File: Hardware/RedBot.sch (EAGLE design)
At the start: 66 parts, among them U1 ATMEGA328P, U2 TB6612FNG, U3 MIC5219 5V, U4 MIC5219 3.3V, U5 FT232RLSSOP, U6 7408SE, Y1 16MHz

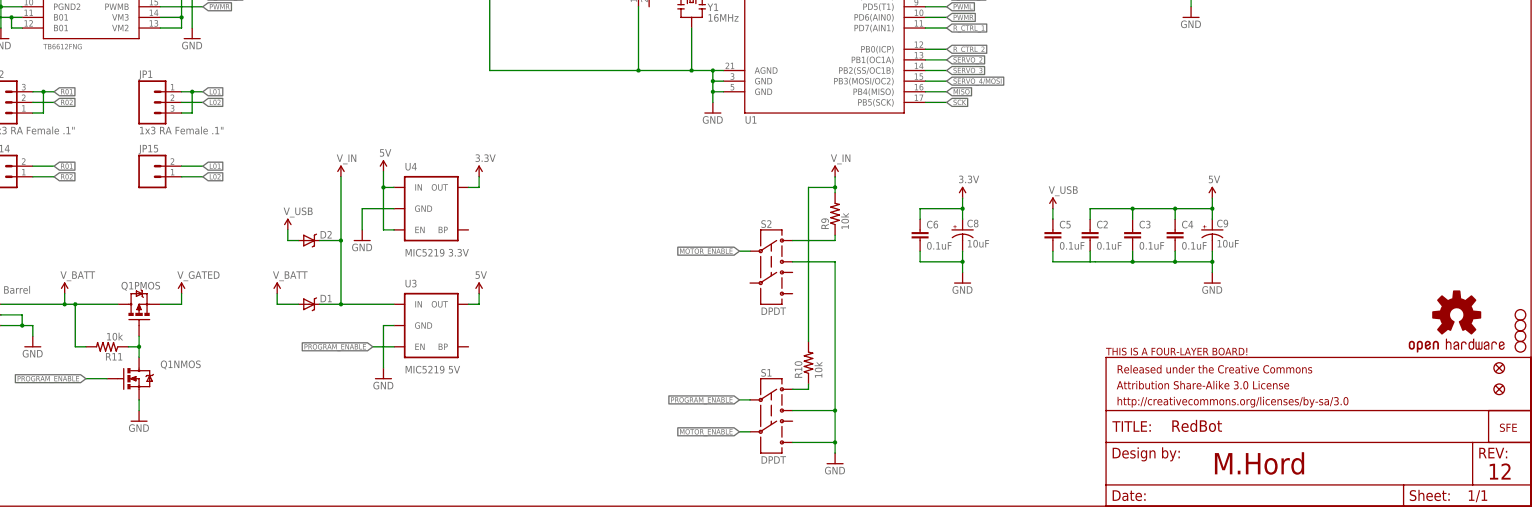
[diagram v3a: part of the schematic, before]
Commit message: Hardware to v13 - Fix gating of battery voltage to servos - Add a user input button to pin 12 - label user led as D13 LED for clarity
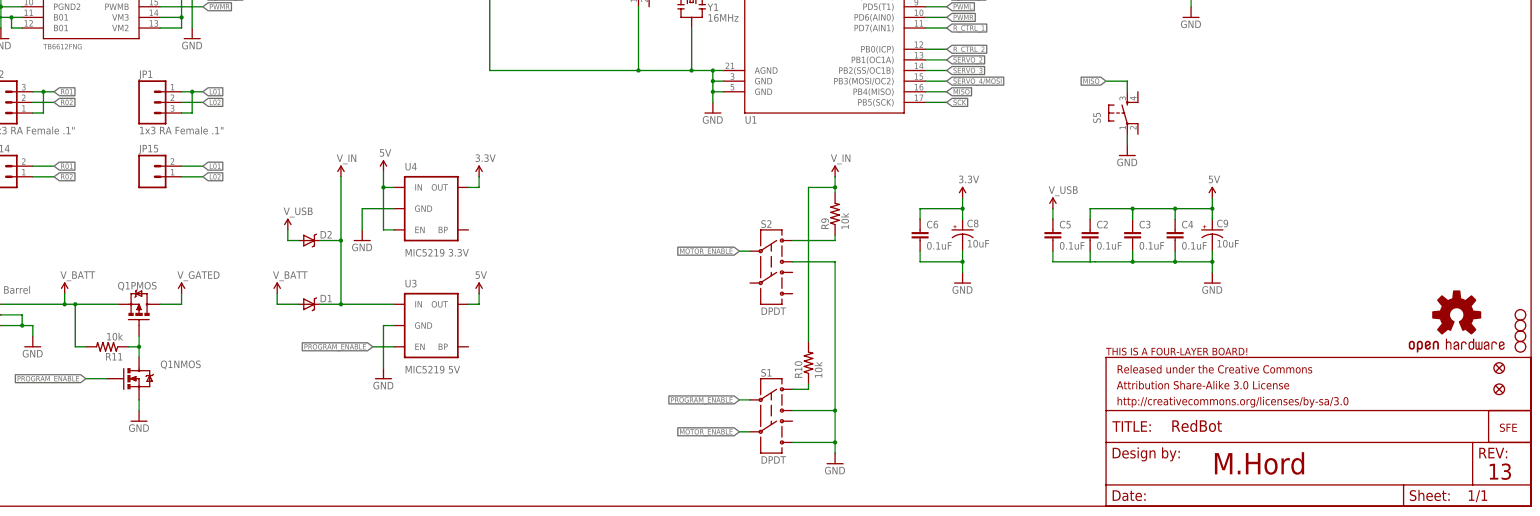
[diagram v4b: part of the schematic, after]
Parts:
- added S5: (no value), SparkFun-Electromechanical:TAC_SWITCHSMD
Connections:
- net GND: now also S5.1
- net MISO: now also S5.3
- net V_BATT: now also Q1PMOS.S; no longer Q1PMOS.D
- net V_GATED: now also Q1PMOS.D; no longer Q1PMOS.S
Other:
- note added: "13"
- note removed: "12"
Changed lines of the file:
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@@
 <part name="FID2" library="SparkFun-Aesthetics" deviceset="FIDUCIAL" device="UFIDUCIAL"/>
 <part name="U$22" library="SparkFun-Aesthetics" deviceset="5V" device="" value="V_USB"/>
+<part name="S5" library="SparkFun-Electromechanical" deviceset="TAC_SWITCH" device="SMD"/>
+<part name="GND12" library="SparkFun-Aesthetics" deviceset="GND" device=""/>
 </parts>
 <sheets>
@@
 <wire x1="0" y1="254" x2="0" y2="0" width="0.1524" layer="94"/>
 <text x="330.2" y="7.62" size="5.08" layer="94">M.Hord</text>
-<text x="395.986" y="6.35" size="3.81" layer="94">12</text>
+<text x="395.986" y="6.35" size="3.81" layer="94">13</text>
 </plain>
 <instances>
@@
 <instance part="JP15" gate="G$1" x="76.2" y="78.74"/>
 <instance part="Q1" gate="NMOS" x="73.66" y="30.48"/>
-<instance part="Q1" gate="PMOS" x="73.66" y="48.26" smashed="yes" rot="R90">
-<attribute name="NAME" x="69.342" y="51.816" size="1.778" layer="95"/>
-<attribute name="VALUE" x="73.66" y="53.34" size="1.778" layer="96" rot="R90"/>
+<instance part="Q1" gate="PMOS" x="73.66" y="48.26" smashed="yes" rot="MR90">
+<attribute name="NAME" x="77.978" y="51.816" size="1.778" layer="95" rot="MR0"/>
+<attribute name="VALUE" x="73.66" y="53.34" size="1.778" layer="96" rot="MR90"/>
 </instance>
 <instance part="GND19" gate="1" x="73.66" y="20.32"/>
@@
 <instance part="FID2" gate="G$1" x="398.78" y="27.94"/>
 <instance part="U$22" gate="G$1" x="144.78" y="195.58"/>
+<instance part="S5" gate="S" x="309.88" y="93.98" rot="R90"/>
+<instance part="GND12" gate="1" x="309.88" y="83.82"/>
 </instances>
 <busses>
@@
 <wire x1="20.32" y1="208.28" x2="15.24" y2="208.28" width="0.1524" layer="91"/>
 <label x="15.24" y="208.28" size="1.27" layer="95" rot="R180" xref="yes"/>
+</segment>
+<segment>
+<pinref part="S5" gate="S" pin="3"/>
+<wire x1="309.88" y1="99.06" x2="309.88" y2="101.6" width="0.1524" layer="91"/>
+<wire x1="309.88" y1="101.6" x2="304.8" y2="101.6" width="0.1524" layer="91"/>
+<label x="304.8" y="101.6" size="1.27" layer="95" rot="R180" xref="yes"/>
 </segment>
 </net>
@@
 <wire x1="27.94" y1="22.86" x2="27.94" y2="20.32" width="0.1524" layer="91"/>
 </segment>
+<segment>
+<pinref part="GND12" gate="1" pin="GND"/>
+<pinref part="S5" gate="S" pin="1"/>
+<wire x1="309.88" y1="86.36" x2="309.88" y2="88.9" width="0.1524" layer="91"/>
+</segment>
 </net>
 <net name="5V" class="0">
@@
 <wire x1="60.96" y1="38.1" x2="58.42" y2="38.1" width="0.1524" layer="91"/>
 <wire x1="58.42" y1="38.1" x2="58.42" y2="48.26" width="0.1524" layer="91"/>
-<pinref part="Q1" gate="PMOS" pin="D"/>
-<wire x1="58.42" y1="48.26" x2="68.58" y2="48.26" width="0.1524" layer="91"/>
-<junction x="58.42" y="48.26"/>
 <wire x1="40.64" y1="48.26" x2="55.88" y2="48.26" width="0.1524" layer="91"/>
 <pinref part="U$18" gate="G$1" pin="V_BATT"/>
@@
 <wire x1="55.88" y1="50.8" x2="55.88" y2="48.26" width="0.1524" layer="91"/>
 <junction x="55.88" y="48.26"/>
+<pinref part="Q1" gate="PMOS" pin="S"/>
+<wire x1="68.58" y1="48.26" x2="58.42" y2="48.26" width="0.1524" layer="91"/>
+<junction x="58.42" y="48.26"/>
 </segment>
 <segment>
@@
 <net name="V_GATED" class="0">
 <segment>
-<pinref part="Q1" gate="PMOS" pin="S"/>
-<wire x1="78.74" y1="48.26" x2="83.82" y2="48.26" width="0.1524" layer="91"/>
 <pinref part="V_GATE1" gate="G$1" pin="V_BATT"/>
 <wire x1="83.82" y1="50.8" x2="83.82" y2="48.26" width="0.1524" layer="91"/>
-</segment>
-<segment>
+<pinref part="Q1" gate="PMOS" pin="D"/>
+<wire x1="78.74" y1="48.26" x2="83.82" y2="48.26" width="0.1524" layer="91"/>
+</segment>
+<segment>

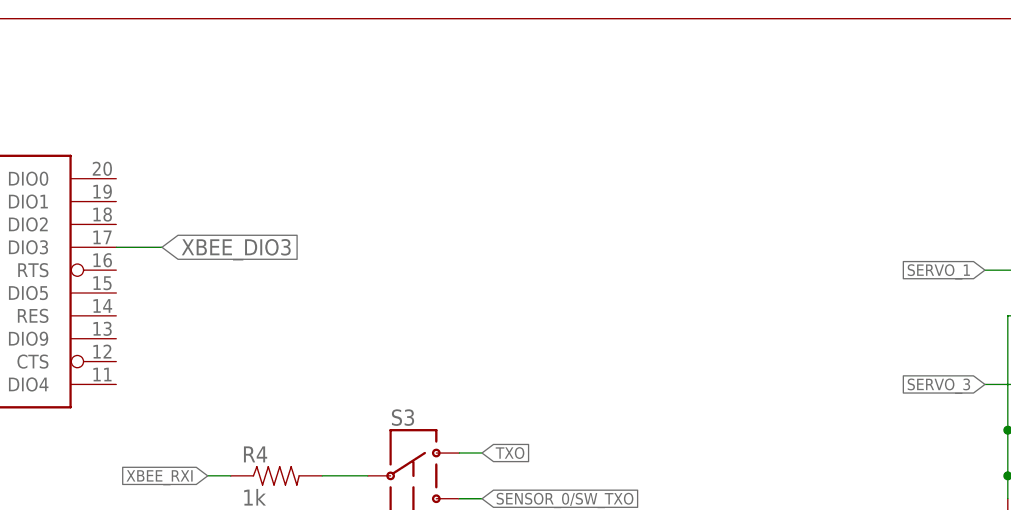
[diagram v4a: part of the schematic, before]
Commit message: Added support for encoder and whisker bumper; changing schematic and layout to fix some issues and pretty it up a bit. Hardware changes not done!
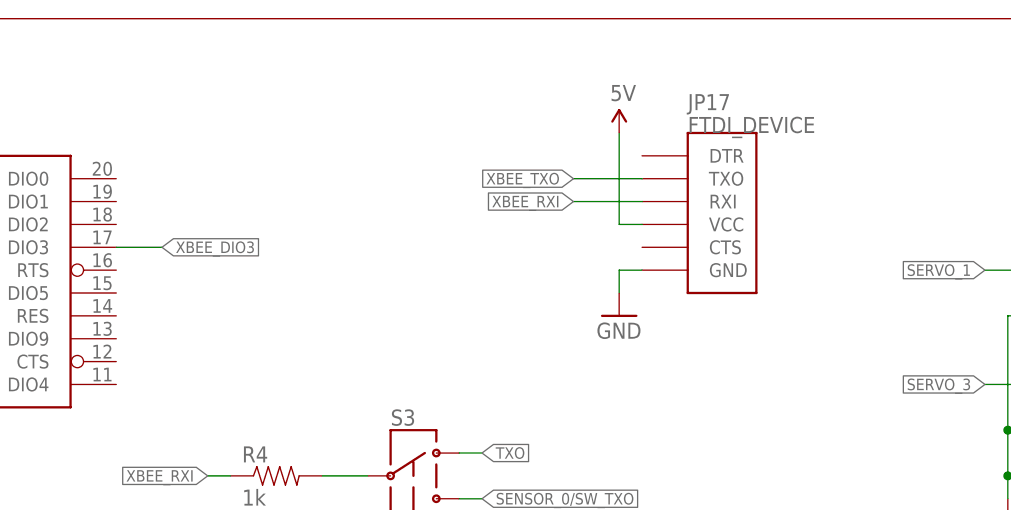
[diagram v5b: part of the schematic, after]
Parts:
- added JP17: FTDI_DEVICE, SparkFun-Connectors:FTDI_DEVICE
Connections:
- net 5V: now also JP17.VCC
- net GND: now also JP17.GND
- net XBEE_RXI: now also JP17.RXI
- net XBEE_TXO: now also JP17.TXO
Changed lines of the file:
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@@
 <layer number="106" name="bPlate" color="7" fill="1" visible="no" active="yes"/>
 <layer number="107" name="Crop" color="7" fill="1" visible="no" active="yes"/>
+<layer number="108" name="tplace-old" color="10" fill="1" visible="yes" active="yes"/>
+<layer number="109" name="ref-old" color="11" fill="1" visible="yes" active="yes"/>
 <layer number="116" name="Patch_BOT" color="9" fill="4" visible="no" active="yes"/>
 <layer number="121" name="_tsilk" color="7" fill="1" visible="no" active="yes"/>
@@
 <part name="S5" library="SparkFun-Electromechanical" deviceset="TAC_SWITCH" device="SMD"/>
 <part name="GND12" library="SparkFun-Aesthetics" deviceset="GND" device=""/>
+<part name="JP17" library="SparkFun-Connectors" deviceset="FTDI_DEVICE" device=""/>
+<part name="GND13" library="SparkFun-Aesthetics" deviceset="GND" device=""/>
+<part name="U$23" library="SparkFun-Aesthetics" deviceset="5V" device=""/>
 </parts>
 <sheets>
@@
 <instance part="S5" gate="S" x="309.88" y="93.98" rot="R90"/>
 <instance part="GND12" gate="1" x="309.88" y="83.82"/>
+<instance part="JP17" gate="G$1" x="289.56" y="233.68"/>
+<instance part="GND13" gate="1" x="281.94" y="220.98"/>
+<instance part="U$23" gate="G$1" x="281.94" y="241.3"/>
 </instances>
 <busses>
@@
 <wire x1="309.88" y1="86.36" x2="309.88" y2="88.9" width="0.1524" layer="91"/>
 </segment>
+<segment>
+<pinref part="JP17" gate="G$1" pin="GND"/>
+<pinref part="GND13" gate="1" pin="GND"/>
+<wire x1="284.48" y1="226.06" x2="281.94" y2="226.06" width="0.1524" layer="91"/>
+<wire x1="281.94" y1="226.06" x2="281.94" y2="223.52" width="0.1524" layer="91"/>
+</segment>
 </net>
 <net name="5V" class="0">
@@
 <junction x="127" y="162.56"/>
 </segment>
+<segment>
+<pinref part="U$23" gate="G$1" pin="5V"/>
+<wire x1="281.94" y1="241.3" x2="281.94" y2="231.14" width="0.1524" layer="91"/>
+<pinref part="JP17" gate="G$1" pin="VCC"/>
+<wire x1="281.94" y1="231.14" x2="284.48" y2="231.14" width="0.1524" layer="91"/>
+</segment>
 </net>
 <net name="V_USB" class="0">
@@
 <label x="236.22" y="195.58" size="1.27" layer="95" rot="R180" xref="yes"/>
 </segment>
+<segment>
+<pinref part="JP17" gate="G$1" pin="TXO"/>
+<wire x1="284.48" y1="236.22" x2="276.86" y2="236.22" width="0.1524" layer="91"/>
+<label x="276.86" y="236.22" size="1.27" layer="95" rot="R180" xref="yes"/>
+</segment>
 </net>
 <net name="XBEE_RXI" class="0">
@@
 <wire x1="238.76" y1="203.2" x2="236.22" y2="203.2" width="0.1524" layer="91"/>
 <label x="236.22" y="203.2" size="1.27" layer="95" rot="R180" xref="yes"/>
+</segment>
+<segment>
+<pinref part="JP17" gate="G$1" pin="RXI"/>
+<wire x1="284.48" y1="233.68" x2="276.86" y2="233.68" width="0.1524" layer="91"/>
+<label x="276.86" y="233.68" size="1.27" layer="95" rot="R180" xref="yes"/>
 </segment>
 </net>
@@
 <pinref part="MOD1" gate="G$1" pin="DIO3"/>
 <wire x1="226.06" y1="228.6" x2="231.14" y2="228.6" width="0.1524" layer="91"/>
-<label x="231.14" y="228.6" size="1.778" layer="95" xref="yes"/>
-</segment>
-<segment>
+<label x="231.14" y="228.6" size="1.27" layer="95" xref="yes"/>
+</segment>
+<segment>

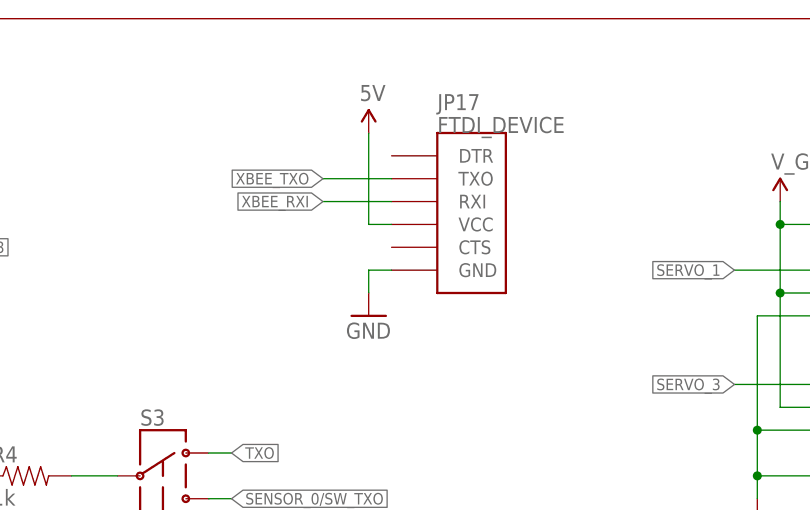
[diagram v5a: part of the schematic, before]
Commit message: Changes to library, changes to board. Will need to do some branching magic to separate the two. This will become the sw dev branch.
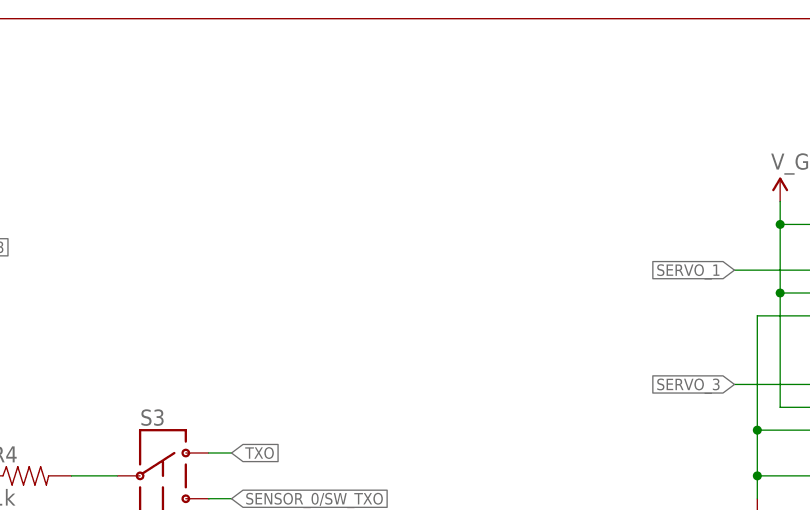
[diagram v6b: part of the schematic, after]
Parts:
- removed JP17: FTDI_DEVICE, SparkFun-Connectors:FTDI_DEVICE
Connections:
- net 5V: no longer JP17.VCC
- net GND: no longer JP17.GND
- net XBEE_RXI: no longer JP17.RXI
- net XBEE_TXO: no longer JP17.TXO
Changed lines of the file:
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@@
 <part name="S5" library="SparkFun-Electromechanical" deviceset="TAC_SWITCH" device="SMD"/>
 <part name="GND12" library="SparkFun-Aesthetics" deviceset="GND" device=""/>
-<part name="JP17" library="SparkFun-Connectors" deviceset="FTDI_DEVICE" device=""/>
-<part name="GND13" library="SparkFun-Aesthetics" deviceset="GND" device=""/>
-<part name="U$23" library="SparkFun-Aesthetics" deviceset="5V" device=""/>
 </parts>
 <sheets>
@@
 <instance part="S5" gate="S" x="309.88" y="93.98" rot="R90"/>
 <instance part="GND12" gate="1" x="309.88" y="83.82"/>
-<instance part="JP17" gate="G$1" x="289.56" y="233.68"/>
-<instance part="GND13" gate="1" x="281.94" y="220.98"/>
-<instance part="U$23" gate="G$1" x="281.94" y="241.3"/>
 </instances>
 <busses>
@@
 <wire x1="309.88" y1="86.36" x2="309.88" y2="88.9" width="0.1524" layer="91"/>
 </segment>
-<segment>
-<pinref part="JP17" gate="G$1" pin="GND"/>
-<pinref part="GND13" gate="1" pin="GND"/>
-<wire x1="284.48" y1="226.06" x2="281.94" y2="226.06" width="0.1524" layer="91"/>
-<wire x1="281.94" y1="226.06" x2="281.94" y2="223.52" width="0.1524" layer="91"/>
-</segment>
 </net>
 <net name="5V" class="0">
@@
 <junction x="127" y="162.56"/>
 </segment>
-<segment>
-<pinref part="U$23" gate="G$1" pin="5V"/>
-<wire x1="281.94" y1="241.3" x2="281.94" y2="231.14" width="0.1524" layer="91"/>
-<pinref part="JP17" gate="G$1" pin="VCC"/>
-<wire x1="281.94" y1="231.14" x2="284.48" y2="231.14" width="0.1524" layer="91"/>
-</segment>
 </net>
 <net name="V_USB" class="0">
@@
 <label x="236.22" y="195.58" size="1.27" layer="95" rot="R180" xref="yes"/>
 </segment>
-<segment>
-<pinref part="JP17" gate="G$1" pin="TXO"/>
-<wire x1="284.48" y1="236.22" x2="276.86" y2="236.22" width="0.1524" layer="91"/>
-<label x="276.86" y="236.22" size="1.27" layer="95" rot="R180" xref="yes"/>
-</segment>
 </net>
 <net name="XBEE_RXI" class="0">
@@
 <label x="236.22" y="203.2" size="1.27" layer="95" rot="R180" xref="yes"/>
 </segment>
-<segment>
-<pinref part="JP17" gate="G$1" pin="RXI"/>
-<wire x1="284.48" y1="233.68" x2="276.86" y2="233.68" width="0.1524" layer="91"/>
-<label x="276.86" y="233.68" size="1.27" layer="95" rot="R180" xref="yes"/>
-</segment>
-</net>
+</net>
